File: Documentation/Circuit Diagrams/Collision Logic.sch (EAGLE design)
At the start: 9 parts, among them IC1 4081D, IC2 4081D, IC3 4081D, IC4 4081D, IC5 4081D

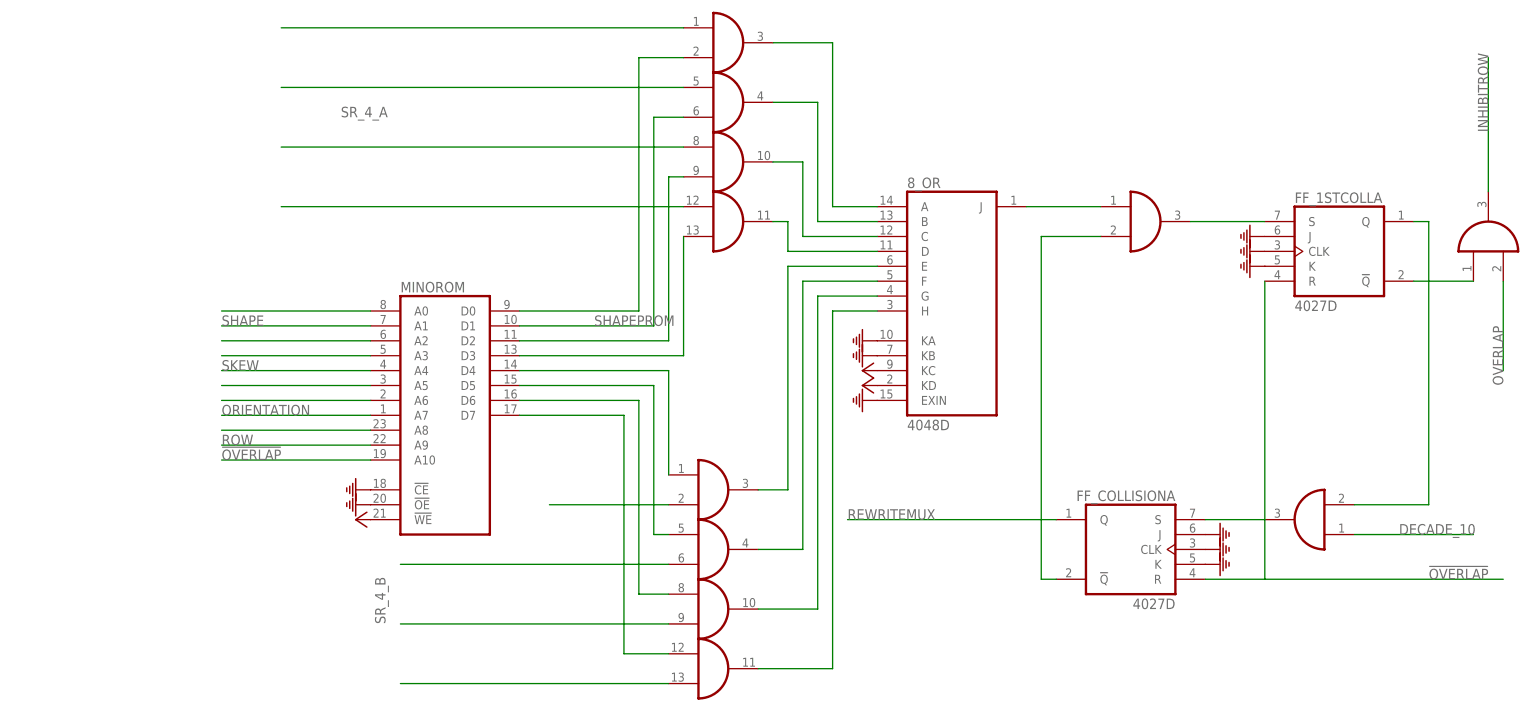
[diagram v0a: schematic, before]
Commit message: PNG export, etc.
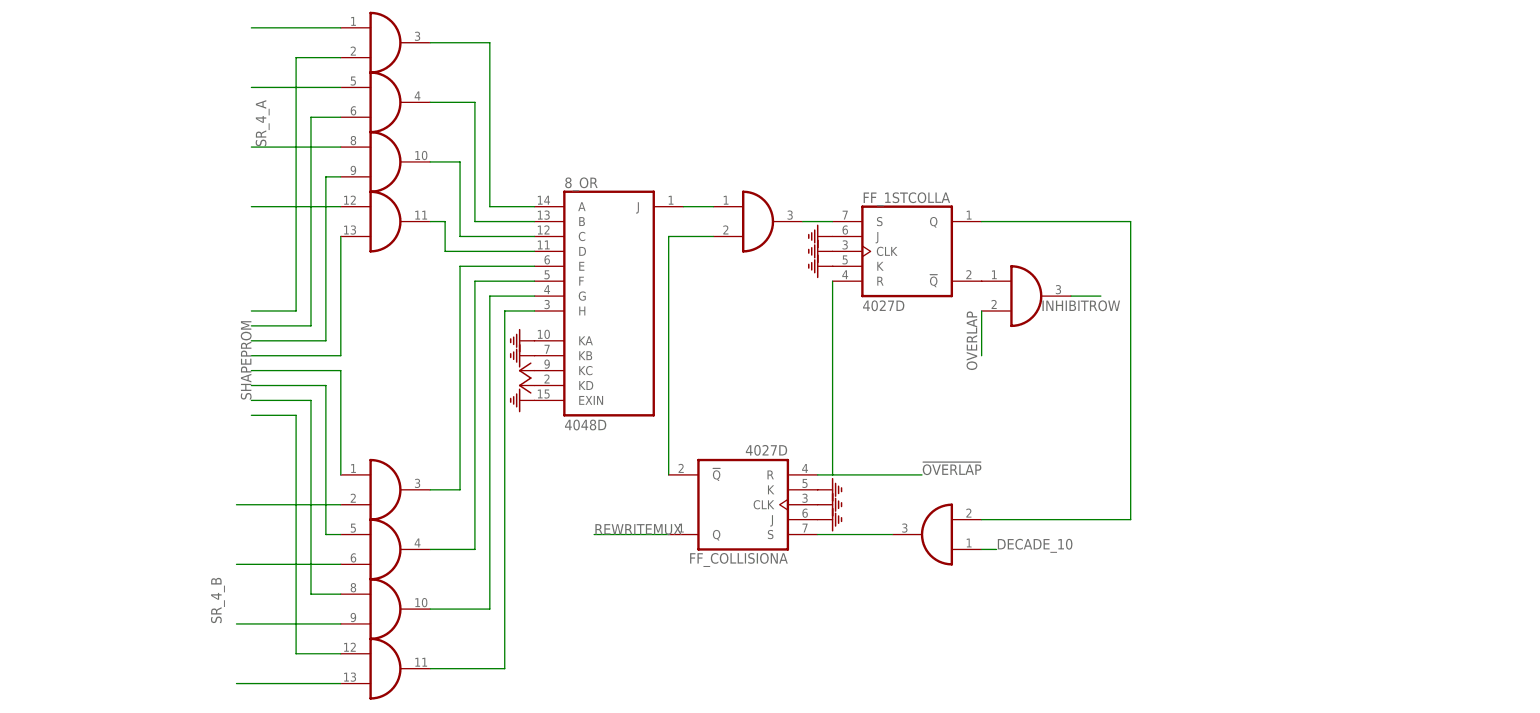
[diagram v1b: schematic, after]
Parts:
- removed MINOROM: (no value), memory:2816
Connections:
- removed net N$14: MINOROMA.A3
- removed net N$16: MINOROMA.A5
- removed net N$24: MINOROMA.A9
- removed net N$25: MINOROMA.A0
- removed net N$27: MINOROMA.A2
- removed net N$5: MINOROMA.A7
- removed net ORIENTATION: MINOROMA.A6
- removed net ROW: MINOROMA.A8
- removed net SHAPE: MINOROMA.A1
- removed net SKEW: MINOROMA.A4
- net !OVERLAP: no longer MINOROMA.A10
- net N$29: no longer MINOROMA.D4
- net N$30: no longer MINOROMA.D0
- net N$31: no longer MINOROMA.D2
- net N$32: no longer MINOROMA.D6
- net N$33: no longer MINOROMA.D7
- net N$34: no longer MINOROMA.D5
- net N$35: no longer MINOROMA.D3
- net PE: no longer MINOROMA.!CE, MINOROMA.!OE
- net SHAPEPROM: no longer MINOROMA.D1
- net V+: no longer MINOROMA.!WE
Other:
- moved on the sheet: 8_OR, FF_1STCOLLA, FF_COLLISIONA

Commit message: Fixed Table Centering, etc.
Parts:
- added BOTTOM: 4002D, 40xx:4002D
- added IC8: 4081D, 40xx:4081D
- added IC9: 4071D, 40xx:4071D
- added NOTEMPTY: 4048D, 40xx:4048D
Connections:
- new net N$14: BOTTOMA.O, IC8A.I1
- new net N$16: IC3A.O, IC9A.I1
- new net N$24: FF_COLLISIONA.S, IC9A.O
- new net N$5: BOTTOMA.I0, BOTTOMA.I1, BOTTOMA.I2
- new net N$7: IC8A.I0, NOTEMPTYA.J
- new net STATE: BOTTOMA.I3
- net N$23: now also IC8A.O, IC9A.I0; no longer FF_COLLISIONA.S, IC3A.O
- net N$29: now also NOTEMPTYA.D
- net N$30: now also NOTEMPTYA.H
- net N$31: now also NOTEMPTYA.F
- net N$32: now also NOTEMPTYA.B
- net N$33: now also NOTEMPTYA.A
- net N$34: now also NOTEMPTYA.C
- net N$35: now also NOTEMPTYA.E
- net PE: now also NOTEMPTYA.EXIN, NOTEMPTYA.KA, NOTEMPTYA.KB
- net SHAPEPROM: now also NOTEMPTYA.G
- net V+: now also NOTEMPTYA.KC, NOTEMPTYA.KD
